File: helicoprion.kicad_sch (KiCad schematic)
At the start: 53 parts, among them J2 TRRS, SW1 SW_SPST, SW10 SW_SPST, SW11 SW_SPST, SW12 SW_SPST, SW13 SW_SPST, SW14 SW_SPST, SW15 SW_SPST, SW16 SW_SPST, SW17 SW_SPST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

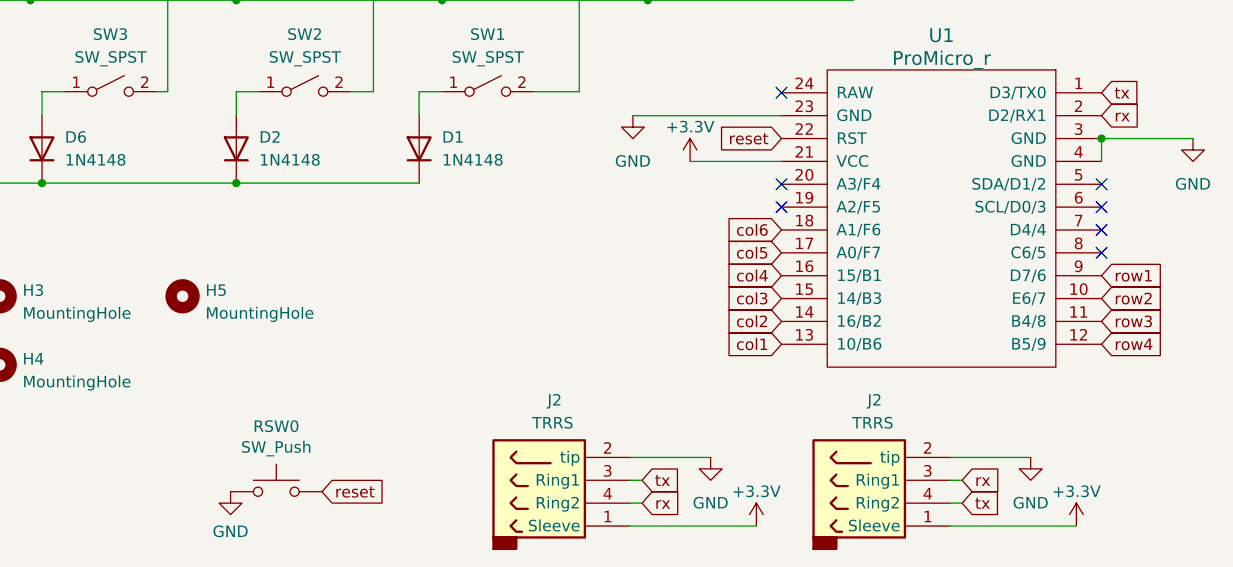
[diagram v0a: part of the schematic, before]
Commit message: start of firmware and interactive bom
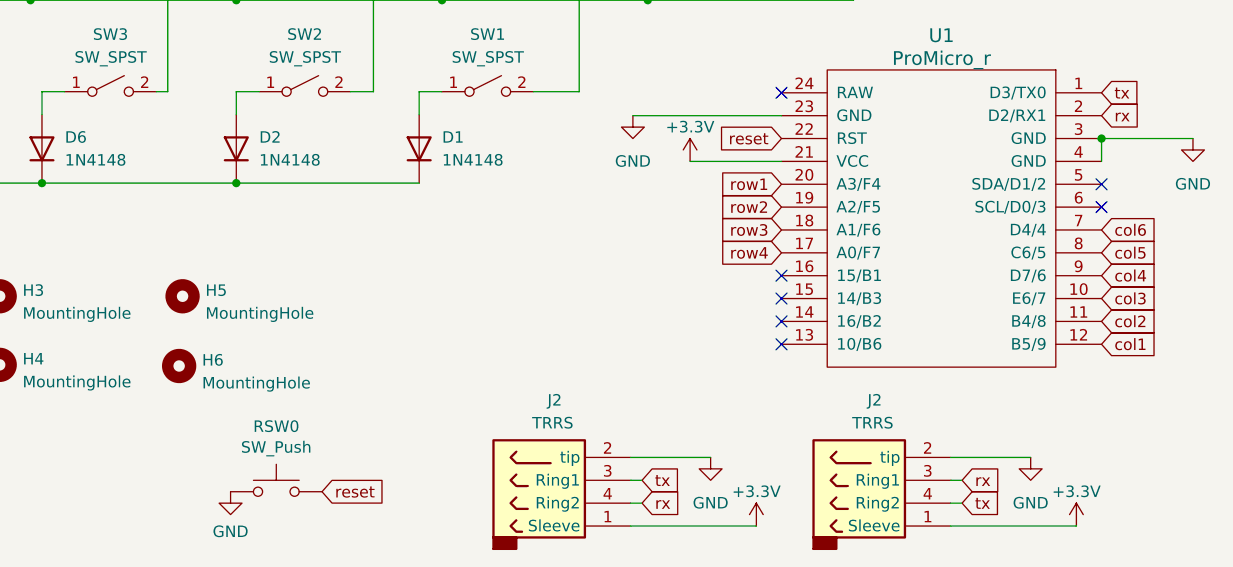
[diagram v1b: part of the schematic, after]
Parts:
- added H6: MountingHole, MountingHole:MountingHole_2.2mm_M2, symbol Mechanical:MountingHole
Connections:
- net col1: now also U1.12 (B5/9); no longer U1.13 (10/B6)
- net col2: now also U1.11 (B4/8); no longer U1.14 (16/B2)
- net col3: now also U1.10 (E6/7); no longer U1.15 (14/B3)
- net col4: now also U1.9 (D7/6); no longer U1.16 (15/B1)
- net col5: now also U1.8 (C6/5); no longer U1.17 (A0/F7)
- net col6: now also U1.7 (D4/4); no longer U1.18 (A1/F6)
- net row1: now also U1.20 (A3/F4); no longer U1.9 (D7/6)
- net row2: now also U1.19 (A2/F5); no longer U1.10 (E6/7)
- net row3: now also U1.18 (A1/F6); no longer U1.11 (B4/8)
- net row4: now also U1.17 (A0/F7); no longer U1.12 (B5/9)
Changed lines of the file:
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@@
   (junction (at 71.12 83.82) (diameter 0) (color 0 0 0 0)
   )
-  (no_connect (at 190.119 109.347))
-  (no_connect (at 190.119 111.887))
+  (no_connect (at 154.559 116.967))
+  (no_connect (at 190.119 106.807))
+  (no_connect (at 154.559 119.507))
   (no_connect (at 154.559 94.107))
-  (no_connect (at 154.559 106.807))
-  (no_connect (at 190.119 106.807))
+  (no_connect (at 154.559 114.427))
+  (no_connect (at 154.559 122.047))
   (no_connect (at 190.119 104.267))
-  (no_connect (at 154.559 104.267))
   (wire (pts (xy 119.38 73.66) (xy 116.84 73.66))
     (stroke (width 0) (type default))
@@
     )
   )
-  (global_label "row4" (shape input) (at 190.119 122.047 0) (fields_autoplaced)
-    (effects (font (size 1.27 1.27)) (justify left))
-    (property "Intersheetrefs" "${INTERSHEET_REFS}" (at 197.5 122.047 0)
+  (global_label "col4" (shape input) (at 190.119 114.427 0) (fields_autoplaced)
+    (effects (font (size 1.27 1.27)) (justify left))
+    (property "Intersheetrefs" "${INTERSHEET_REFS}" (at 197.1371 114.427 0)
       (effects (font (size 1.27 1.27)) (justify left) hide)
     )
@@
     )
   )
-  (global_label "col3" (shape input) (at 154.559 116.967 180) (fields_autoplaced)
-    (effects (font (size 1.27 1.27)) (justify right))
-    (property "Intersheetrefs" "${INTERSHEET_REFS}" (at 147.5409 116.967 0)
-      (effects (font (size 1.27 1.27)) (justify right) hide)
-    )
-  )
-  (global_label "col6" (shape input) (at 154.559 109.347 180) (fields_autoplaced)
-    (effects (font (size 1.27 1.27)) (justify right))
-    (property "Intersheetrefs" "${INTERSHEET_REFS}" (at 147.5409 109.347 0)
-      (effects (font (size 1.27 1.27)) (justify right) hide)
-    )
-  )
   (global_label "rx" (shape input) (at 174.625 137.16 0) (fields_autoplaced)
     (effects (font (size 1.27 1.27)) (justify left))
@@
     )
   )
-  (global_label "col4" (shape input) (at 154.559 114.427 180) (fields_autoplaced)
-    (effects (font (size 1.27 1.27)) (justify right))
-    (property "Intersheetrefs" "${INTERSHEET_REFS}" (at 147.5409 114.427 0)
-      (effects (font (size 1.27 1.27)) (justify right) hide)
+  (global_label "col6" (shape input) (at 190.119 109.347 0) (fields_autoplaced)
+    (effects (font (size 1.27 1.27)) (justify left))
+    (property "Intersheetrefs" "${INTERSHEET_REFS}" (at 197.1371 109.347 0)
+      (effects (font (size 1.27 1.27)) (justify left) hide)
     )
   )
@@
     )
   )
-  (global_label "col1" (shape input) (at 154.559 122.047 180) (fields_autoplaced)
+  (global_label "col2" (shape input) (at 86.36 25.4 90) (fields_autoplaced)
+    (effects (font (size 1.27 1.27)) (justify left))
+    (property "Intersheetrefs" "${INTERSHEET_REFS}" (at 86.36 18.3819 90)
+      (effects (font (size 1.27 1.27)) (justify left) hide)
+    )
+  )
+  (global_label "tx" (shape input) (at 174.625 139.7 0) (fields_autoplaced)
+    (effects (font (size 1.27 1.27)) (justify left))
+    (property "Intersheetrefs" "${INTERSHEET_REFS}" (at 178.7919 139.6206 0)
+      (effects (font (size 1.27 1.27)) (justify left) hide)
+    )
+  )
+  (global_label "col3" (shape input) (at 190.119 116.967 0) (fields_autoplaced)
+    (effects (font (size 1.27 1.27)) (justify left))
+    (property "Intersheetrefs" "${INTERSHEET_REFS}" (at 197.1371 116.967 0)
+      (effects (font (size 1.27 1.27)) (justify left) hide)
+    )
+  )
+  (global_label "row3" (shape input) (at 154.559 109.347 180) (fields_autoplaced)
     (effects (font (size 1.27 1.27)) (justify right))
-    (property "Intersheetrefs" "${INTERSHEET_REFS}" (at 147.5409 122.047 0)
+    (property "Intersheetrefs" "${INTERSHEET_REFS}" (at 147.178 109.347 0)
       (effects (font (size 1.27 1.27)) (justify right) hide)
     )
   )
-  (global_label "col2" (shape input) (at 86.36 25.4 90) (fields_autoplaced)
-    (effects (font (size 1.27 1.27)) (justify left))
-    (property "Intersheetrefs" "${INTERSHEET_REFS}" (at 86.36 18.3819 90)
-      (effects (font (size 1.27 1.27)) (justify left) hide)
-    )
-  )
-  (global_label "tx" (shape input) (at 174.625 139.7 0) (fields_autoplaced)
-    (effects (font (size 1.27 1.27)) (justify left))
-    (property "Intersheetrefs" "${INTERSHEET_REFS}" (at 178.7919 139.6206 0)
-      (effects (font (size 1.27 1.27)) (justify left) hide)
-    )
-  )
-  (global_label "row3" (shape input) (at 190.119 119.507 0) (fields_autoplaced)
-    (effects (font (size 1.27 1.27)) (justify left))
-    (property "Intersheetrefs" "${INTERSHEET_REFS}" (at 197.0073 119.4276 0)
-      (effects (font (size 1.27 1.27)) (justify left) hide)
+  (global_label "row4" (shape input) (at 154.559 111.887 180) (fields_autoplaced)
+    (effects (font (size 1.27 1.27)) (justify right))
+    (property "Intersheetrefs" "${INTERSHEET_REFS}" (at 147.178 111.887 0)
+      (effects (font (size 1.27 1.27)) (justify right) hide)
     )
   )
@@
     )
   )
-  (global_label "row1" (shape input) (at 190.119 114.427 0) (fields_autoplaced)
-    (effects (font (size 1.27 1.27)) (justify left))
-    (property "Intersheetrefs" "${INTERSHEET_REFS}" (at 197.0073 114.3476 0)
-      (effects (font (size 1.27 1.27)) (justify left) hide)
-    )
-  )
-  (global_label "col5" (shape input) (at 154.559 111.887 180) (fields_autoplaced)
+  (global_label "col1" (shape input) (at 190.119 122.047 0) (fields_autoplaced)
+    (effects (font (size 1.27 1.27)) (justify left))
+    (property "Intersheetrefs" "${INTERSHEET_REFS}" (at 197.1371 122.047 0)
+      (effects (font (size 1.27 1.27)) (justify left) hide)
+    )
+  )
+  (global_label "row2" (shape input) (at 154.559 106.807 180) (fields_autoplaced)
     (effects (font (size 1.27 1.27)) (justify right))
-    (property "Intersheetrefs" "${INTERSHEET_REFS}" (at 147.5409 111.887 0)
+    (property "Intersheetrefs" "${INTERSHEET_REFS}" (at 147.178 106.807 0)
       (effects (font (size 1.27 1.27)) (justify right) hide)
     )
   )
+  (global_label "row1" (shape input) (at 154.559 104.267 180) (fields_autoplaced)
+    (effects (font (size 1.27 1.27)) (justify right))
+    (property "Intersheetrefs" "${INTERSHEET_REFS}" (at 147.178 104.267 0)
+      (effects (font (size 1.27 1.27)) (justify right) hide)
+    )
+  )
+  (global_label "col2" (shape input) (at 190.119 119.507 0) (fields_autoplaced)
+    (effects (font (size 1.27 1.27)) (justify left))
+    (property "Intersheetrefs" "${INTERSHEET_REFS}" (at 197.1371 119.507 0)
+      (effects (font (size 1.27 1.27)) (justify left) hide)
+    )
+  )
+  (global_label "col5" (shape input) (at 190.119 111.887 0) (fields_autoplaced)
+    (effects (font (size 1.27 1.27)) (justify left))
+    (property "Intersheetrefs" "${INTERSHEET_REFS}" (at 197.1371 111.887 0)
+      (effects (font (size 1.27 1.27)) (justify left) hide)
+    )
+  )
   (global_label "tx" (shape input) (at 190.119 94.107 0) (fields_autoplaced)
     (effects (font (size 1.27 1.27)) (justify left))
@@
     (property "Intersheetrefs" "${INTERSHEET_REFS}" (at 154.94 18.3819 90)
       (effects (font (size 1.27 1.27)) (justify left) hide)
-    )
-  )
-  (global_label "col2" (shape input) (at 154.559 119.507 180) (fields_autoplaced)
-    (effects (font (size 1.27 1.27)) (justify right))
-    (property "Intersheetrefs" "${INTERSHEET_REFS}" (at 147.5409 119.507 0)
-      (effects (font (size 1.27 1.27)) (justify right) hide)
     )
   )
@@
     )
   )
-  (global_label "row2" (shape input) (at 190.119 116.967 0) (fields_autoplaced)
-    (effects (font (size 1.27 1.27)) (justify left))
-    (property "Intersheetrefs" "${INTERSHEET_REFS}" (at 197.0073 116.8876 0)
-      (effects (font (size 1.27 1.27)) (justify left) hide)
-    )
-  )
   (global_label "reset" (shape input) (at 103.505 138.43 0) (fields_autoplaced)
     (effects (font (size 1.27 1.27)) (justify left))
@@
         )
       )
+    )
+  )
+  (symbol (lib_id "Mechanical:MountingHole") (at 87.63 124.46 0) (unit 1)
+    (in_bom yes) (on_board yes) (dnp no) (fields_autoplaced)
+    (property "Reference" "H6" (at 90.17 123.825 0)
+      (effects (font (size 1.27 1.27)) (justify left))
+    )
+    (property "Value" "MountingHole" (at 90.17 126.365 0)
+      (effects (font (size 1.27 1.27)) (justify left))
+    )
+    (property "Footprint" "MountingHole:MountingHole_2.2mm_M2" (at 87.63 124.46 0)
+      (effects (font (size 1.27 1.27)) hide)
+    )
+    (property "Datasheet" "~" (at 87.63 124.46 0)
+      (effects (font (size 1.27 1.27)) hide)
+    )
+    (instances
+      (project "helicoprion"
+        (path "/aecf1c42-e4b0-4cf8-84e5-d322673cbacc"
+          (reference "H6") (unit 1)
+        )
+      )
